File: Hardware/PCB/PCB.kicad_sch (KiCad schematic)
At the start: 2 parts, among them P1 USB_C_Plug_USB2.0, U1 ESP32-H2-MINI-1

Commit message: Playing with LDOs
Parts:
- added U2: SPX3819M5-L-3-3, Package_TO_SOT_SMD:SOT-23-5, symbol Regulator_Linear:SPX3819M5-L-3-3
- added U3: AMS1117-3.3, Package_TO_SOT_SMD:SOT-223-3_TabPin2, symbol Regulator_Linear:AMS1117-3.3
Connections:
- net GND: now reaches U1.1 (GND), U1.11 (GND), U1.14 (GND), U1.2 (GND), U1.36 (GND), U1.37 (GND), U1.38 (GND), U1.39 (GND), U1.40 (GND), U1.41 (GND), U1.42 (GND), U1.43 (GND), U1.44 (GND), U1.45 (GND), U1.46 (GND), U1.47 (GND), U1.48 (GND), U1.49 (GND), U1.50 (GND), U1.51 (GND), U1.52 (GND), U1.53 (GND)
- net GND: now also P1.A1 (GND), P1.A12 (GND), P1.B1 (GND), P1.B12 (GND), U3.1 (GND)
- net USB_D-: now reaches U1.26 (GPIO26/FSPICS4/USB_D-)
- net USB_D-: now also P1.A7 (D-)
- net USB_D+: now reaches U1.27 (GPIO27/FSPICS5/USB_D+)
- net USB_D+: now also P1.A6 (D+)
- net at U1.3 (3V3): now also U3.2 (VO)
- net at P1.A4 (VBUS), P1.A9 (VBUS), P1.B4 (VBUS)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: now also U3.3 (VI)
- no-connect marks 0 -> 18

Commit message: First pass at full layout
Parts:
- removed P1: USB_C_Plug_USB2.0, Connector_USB:USB_C_Receptacle_GCT_USB4135-GF-A_6P_TopMnt_Horizontal, symbol Connector:USB_C_Plug_USB2.0
- removed U2: SPX3819M5-L-3-3, Package_TO_SOT_SMD:SOT-23-5, symbol Regulator_Linear:SPX3819M5-L-3-3
- removed U3: AMS1117-3.3, Package_TO_SOT_SMD:SOT-223-3_TabPin2, symbol Regulator_Linear:AMS1117-3.3
- added C1: 10µ, Capacitor_SMD:C_0805_2012Metric, symbol Device:C
- added C2, C7: 1µF, Capacitor_SMD:C_0805_2012Metric, symbol Device:C
- added C3: 0.1µ, Capacitor_SMD:C_0805_2012Metric, symbol Device:C
- added C5: 1µ, Capacitor_SMD:C_0805_2012Metric, symbol Device:C
- added D1, D2, D3: LED, LED_SMD:LED_0805_2012Metric, symbol Device:LED
- added J1: USB_C_Receptacle_USB2.0_14P, Connector_USB:USB_C_Receptacle_GCT_USB4110, symbol Connector:USB_C_Receptacle_USB2.0_14P
- added J2: Conn_01x08_Pin, Connector_PinHeader_2.54mm:PinHeader_1x08_P2.54mm_Vertical, symbol Connector:Conn_01x08_Pin
- added J3: Conn_01x8_Pin, Connector_PinHeader_2.54mm:PinHeader_1x08_P2.54mm_Vertical, symbol Connector:Conn_01x08_Pin
- added R1, R2, R4, R5, R6: 5.1K, Resistor_SMD:R_0805_2012Metric, symbol Device:R
- added R3: 10K, Resistor_SMD:R_0805_2012Metric, symbol Device:R
- added SW1, SW2: SW_Push, Button_Switch_SMD:SW_SPST_TS-1088-xR025, symbol Switch:SW_Push
- added U3: MCP1700x-330xxTT, Package_TO_SOT_SMD:SOT-23, symbol Regulator_Linear:MCP1700x-330xxTT
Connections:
- net GND: now also C1.2, C2.2, C3.2, C5.2, C7.2, D1.1 (K), D2.1 (K), D3.1 (K), J1.A1 (GND), J1.A12 (GND), J1.B1 (GND), J1.B12 (GND), J1.S1 (SHIELD), J2.1 (Pin_1), R1.2, R2.2, SW1.1, SW2.1, U3.1 (GND)
- net USB_D+: now also J1.A6 (D+), J1.B6 (D+)
- net USB_D-: now also J1.A7 (D-), J1.B7 (D-)
- net +3.3V: now reaches U1.3 (3V3)
- net +3.3V: now also C1.1, C2.1, C3.1, J2.2 (Pin_2), R3.1, R5.1, U3.2 (VO)
- net GPIO1: now reaches U1.10 (GPIO1/FSPICS0/ADC1_CH0)
- net GPIO1: now also J2.5 (Pin_5)
- net GPIO13: now reaches U1.12 (GPIO13/XTAL_32K_P)
- net GPIO13: now also J2.6 (Pin_6)
- net GPIO14: now reaches U1.13 (GPIO14/XTAL_32K_N)
- net GPIO14: now also J2.7 (Pin_7)
- net GPIO12: now reaches U1.16 (GPIO12)
- net GPIO12: now also J2.8 (Pin_8)
- net GPIO4: now reaches U1.18 (GPIO4/FSPICLK/ADC1_CH3/MTCK)
- net GPIO4: now also R6.1
- net GPIO5: now reaches U1.19 (GPIO5/FSPID/ADC1_CH4/MTDI)
- net GPIO5: now also J3.8 (Pin_8)
- net GPIO10: now reaches U1.20 (GPIO10/ZCD0)
- net GPIO10: now also J3.7 (Pin_7)
- net GPIO11: now reaches U1.21 (GPIO11/ZCD1)
- net GPIO11: now also J3.6 (Pin_6)
- net GPIO8: now reaches U1.22 (GPIO8)
- net GPIO8: now also J3.5 (Pin_5)
- net GPIO9: now reaches U1.23 (GPIO9)
- net GPIO9: now also J3.4 (Pin_4)
- net GPIO22: now reaches U1.24 (GPIO22)
- net GPIO22: now also J3.3 (Pin_3)
- net GPIO25: now reaches U1.25 (GPIO25/FSPICS3)
- net GPIO25: now also J3.2 (Pin_2)
- net GPIO23: now reaches U1.30 (GPIO23/FSPICS1/U0RXD)
- net GPIO24: now reaches U1.31 (GPIO24/FSPICS2/U0TXD)
- net GPIO2: now reaches U1.5 (GPIO2/FSPIWP/ADC1_CH1/MTMS)
- net GPIO2: now also J2.3 (Pin_3)
- net GPIO3: now reaches U1.6 (GPIO3/FSPIHD/ADC1_CH2/MTDO)
- net GPIO3: now also J2.4 (Pin_4)
- net EN: now reaches U1.8 (EN)
- net EN: now also C5.1, R3.2, SW1.2
- net BOOT: now reaches U1.9 (GPIO0/FSPIQ)
- net BOOT: now also SW2.2
- new net: J1.A5 (CC1), R2.1
- new net: J1.B5 (CC2), R1.1
- new net: D2.2 (A), R5.2
- new net: D1.2 (A), R4.2
- new net: D3.2 (A), R6.2
- new net +5V: C7.1, J1.A4 (VBUS), J1.A9 (VBUS), J1.B4 (VBUS), J1.B9 (VBUS), J3.1 (Pin_1), R4.1, U3.3 (VI)
- no-connect marks 18 -> 1
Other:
- title: (none) -> ESP32-H2 DevKit
- moved on the sheet: U1

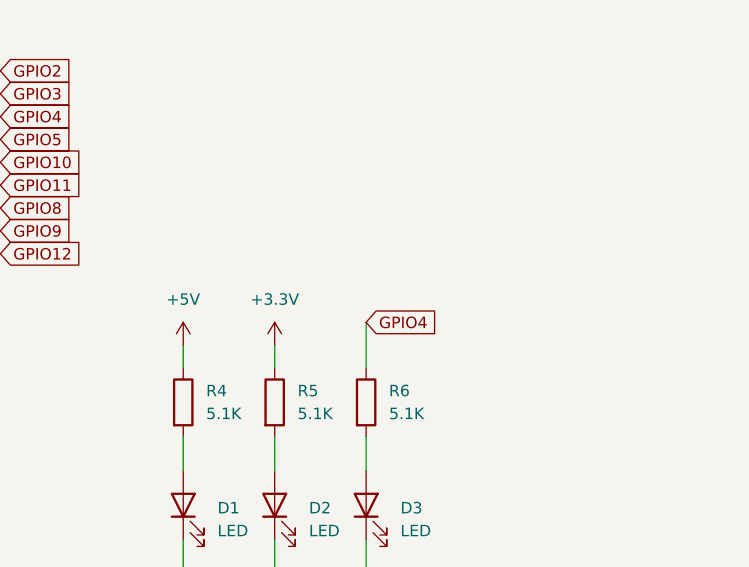
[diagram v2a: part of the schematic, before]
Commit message: Finished PCB layout
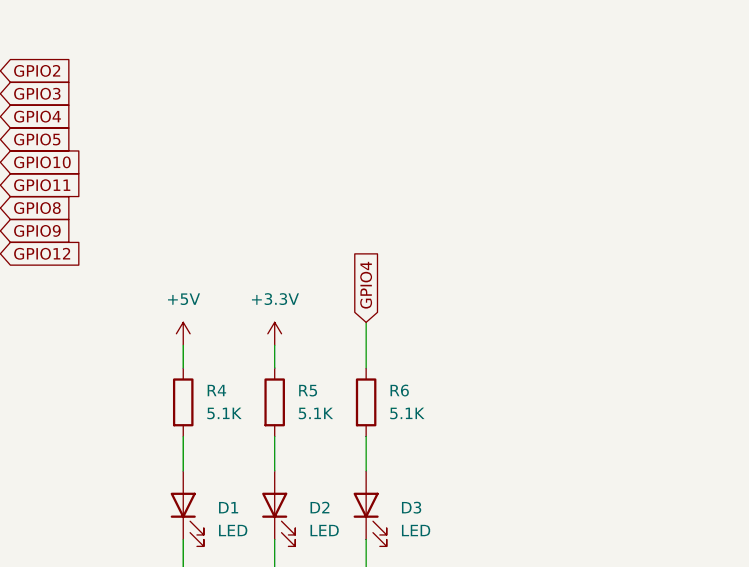
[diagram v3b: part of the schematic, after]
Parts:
- J1: footprint Connector_USB:USB_C_Receptacle_GCT_USB4110 -> Connector_USB:USB_C_Receptacle_GCT_USB4105-xx-A_16P_TopMnt_Horizontal
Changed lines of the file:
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@@
 	(global_label "GPIO4"
 		(shape input)
-		(at 236.22 123.19 0)
-		(fields_autoplaced yes)
-		(effects
-			(font
-				(size 1.27 1.27)
-			)
-			(justify left)
-		)
-		(property "Intersheetrefs" "${INTERSHEET_REFS}"
-			(at 244.89 123.19 0)
+		(at 236.22 123.19 90)
+		(fields_autoplaced yes)
+		(effects
+			(font
+				(size 1.27 1.27)
+			)
+			(justify left)
+		)
+		(property "Intersheetrefs" "${INTERSHEET_REFS}"
+			(at 236.22 114.52 90)
 			(effects
 				(font
@@
 			)
 		)
-		(property "Footprint" "Connector_USB:USB_C_Receptacle_GCT_USB4110"
+		(property "Footprint" "Connector_USB:USB_C_Receptacle_GCT_USB4105-xx-A_16P_TopMnt_Horizontal"
 			(at 38.1 95.25 0)
 			(effects

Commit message: Fixed up RC capacitor order
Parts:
- renumbered C3 to C1, C1 to C2, C2 to C3
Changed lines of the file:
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@@
 	(title_block
 		(title "ESP32-H2 DevKit")
+		(rev "1")
 	)
 	(junction
@@
 		(dnp no)
 		(fields_autoplaced yes)
-		(property "Reference" "C2"
+		(property "Reference" "C3"
 			(at 77.47 166.3699 0)
 			(effects
@@
 			(project "PCB"
 				(path "/dce6804a-3b58-43ff-b96d-51bc6b062a66"
-					(reference "C2")
+					(reference "C3")
 					(unit 1)
 				)
@@
 		(dnp no)
 		(fields_autoplaced yes)
-		(property "Reference" "C3"
+		(property "Reference" "C1"
 			(at 102.87 166.3699 0)
 			(effects
@@
 			(project "PCB"
 				(path "/dce6804a-3b58-43ff-b96d-51bc6b062a66"
-					(reference "C3")
+					(reference "C1")
 					(unit 1)
 				)
@@
 		(dnp no)
 		(fields_autoplaced yes)
-		(property "Reference" "C1"
+		(property "Reference" "C2"
 			(at 90.17 166.3699 0)
 			(effects
@@
 			(project "PCB"
 				(path "/dce6804a-3b58-43ff-b96d-51bc6b062a66"
-					(reference "C1")
+					(reference "C2")
 					(unit 1)
 				)
